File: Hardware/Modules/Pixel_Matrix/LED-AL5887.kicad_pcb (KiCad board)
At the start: 2 copper layers, 35 x 35 mm, 50 parts, among them J1 B4B-EH-A, J2 Conn_01x03_Pin, J3 Conn_01x03_Pin, J4 Conn_01x03_Pin, J5 B6B-EH-A, U1 AL5887JAZW52-13

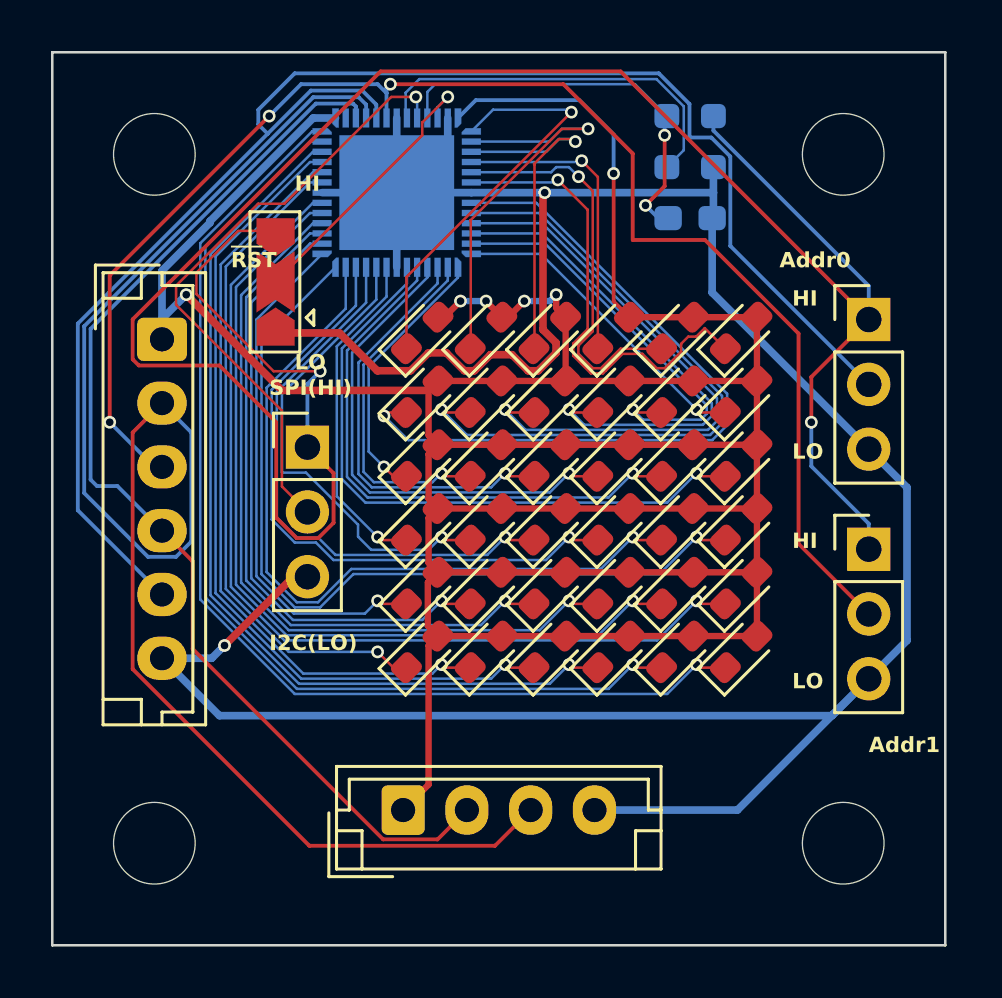
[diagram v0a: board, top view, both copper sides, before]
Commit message: Updated silkscreen
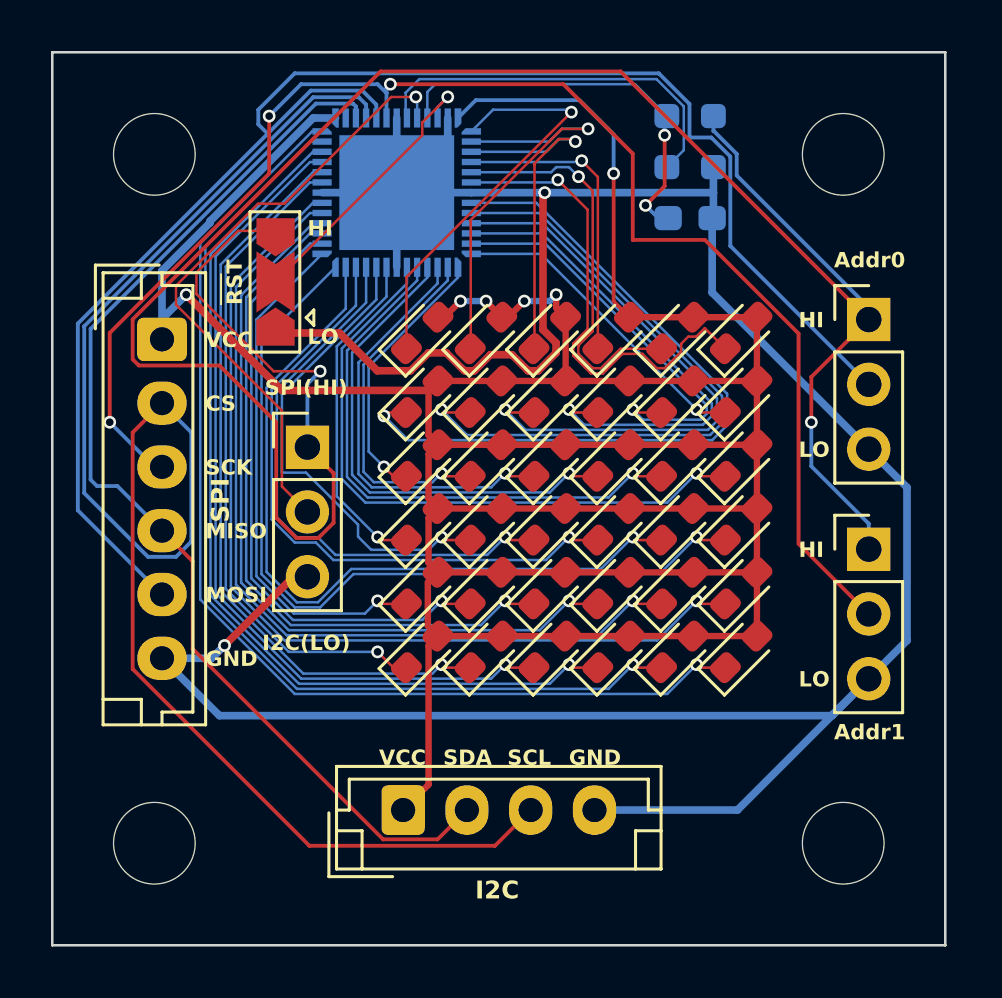
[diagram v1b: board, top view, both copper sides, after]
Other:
- board text added: "C1"
- board text added: "CS"
- board text added: "GND"
- board text added: "I2C"
- board text added: "MISO"
- board text added: "MOSI"
- board text added: "R1"
- board text added: "R2"
- board text added: "SCK"
- board text added: "SCL"
- board text added: "SDA"
- board text added: "SPI"
- board text added: "VCC"

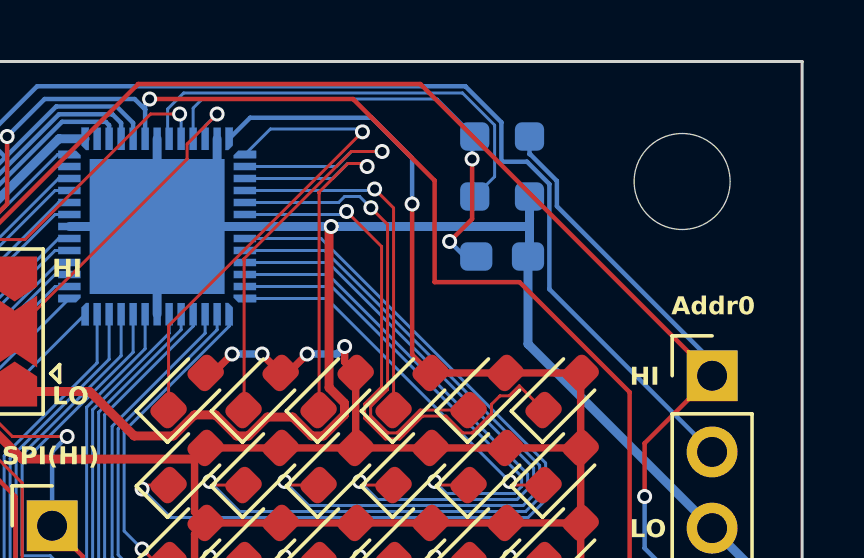
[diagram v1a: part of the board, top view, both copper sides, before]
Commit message: Pin 51 gefixt
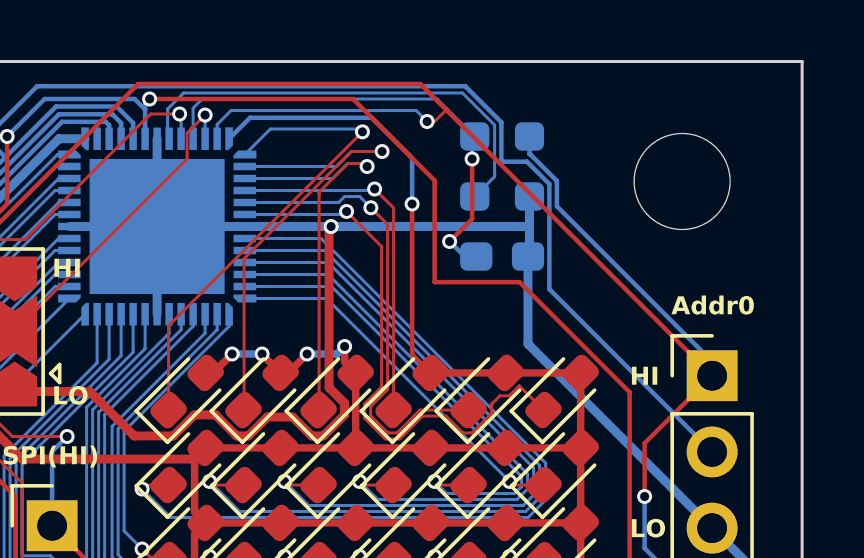
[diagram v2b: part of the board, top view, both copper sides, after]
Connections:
- U1 pad 51: GND -> Net-(J2-Pin_1)
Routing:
- net Net-(J2-Pin_1): track 90.4 -> 99.0 mm, vias 2 -> 3
- net GND: track 117.5 -> 116.5 mm
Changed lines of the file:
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@@
 			(size 0.25 0.75)
 			(layers "B.Cu" "B.Paste")
-			(net 5 "GND")
+			(net 47 "Net-(J2-Pin_1)")
 			(pinfunction "~{EN}")
 			(pintype "input")
@@
 	)
 	(segment
-		(start 74.5 34.075)
-		(end 74.5 35)
-		(width 0.3)
-		(layer "B.Cu")
-		(net 5)
-	)
-	(segment
 		(start 75.425 37)
 		(end 78.3 37)
@@
 	)
 	(segment
+		(start 91 41.975)
+		(end 82.1375 33.1125)
+		(width 0.15)
+		(layer "F.Cu")
+		(net 47)
+	)
+	(segment
 		(start 81.275 32.25)
 		(end 71.867032 32.25)
@@
 	)
 	(segment
-		(start 91 41.975)
-		(end 81.275 32.25)
-		(width 0.15)
+		(start 81.75 33.5)
+		(end 82.1375 33.1125)
+		(width 0.1)
 		(layer "F.Cu")
 		(net 47)
@@
 	)
 	(segment
+		(start 81.5 33.5)
+		(end 81.75 33.5)
+		(width 0.1)
+		(layer "F.Cu")
+		(net 47)
+	)
+	(segment
 		(start 69.424569 50.54)
 		(end 70.025 49.939569)
@@
 	)
 	(segment
+		(start 82.1375 33.1125)
+		(end 81.275 32.25)
+		(width 0.15)
+		(layer "F.Cu")
+		(net 47)
+	)
+	(segment
 		(start 68.575431 50.54)
 		(end 69.424569 50.54)
@@
 	)
 	(via
+		(at 81.5 33.5)
+		(size 0.5)
+		(drill 0.3)
+		(layers "F.Cu" "B.Cu")
+		(net 47)
+	)
+	(via
 		(at 88.75 46)
 		(size 0.5)
@@
 	)
 	(segment
+		(start 74.5 33.6)
+		(end 74.5 34.075)
+		(width 0.1)
+		(layer "B.Cu")
+		(net 47)
+	)
+	(segment
 		(start 84.9125 34)
 		(end 84.9125 34.589944)
@@
 	)
 	(segment
+		(start 74.965012 33.134988)
+		(end 74.5 33.6)
+		(width 0.1)
+		(layer "B.Cu")
+		(net 47)
+	)
+	(segment
 		(start 91 50.975)
 		(end 91 49.975)
@@
 	)
 	(segment
+		(start 81.134988 33.134988)
+		(end 74.965012 33.134988)
+		(width 0.1)
+		(layer "B.Cu")
+		(net 47)
+	)
+	(segment
 		(start 85.825 36.325)
 		(end 91 41.5)
@@
 	)
 	(segment
+		(start 81.5 33.5)
+		(end 81.134988 33.134988)
+		(width 0.1)
+		(layer "B.Cu")
+		(net 47)
+	)
+	(segment
 		(start 84.933442 34.589944)
 		(end 85.825 35.481502)
@@
 	)
 	(segment
-		(start 73.5 34.25)
-		(end 73.5 34.75)
+		(start 73.5 34.75)
+		(end 67.75 40.5)
 		(width 0.1)
 		(layer "F.Cu")
@@
 	)
 	(segment
-		(start 74.5 33.25)
-		(end 73.5 34.25)
+		(start 74.1 33.285356)
+		(end 73.5 33.885356)
 		(width 0.1)
 		(layer "F.Cu")
@@
 	)
 	(segment
-		(start 73.5 34.75)
-		(end 67.75 40.5)
+		(start 73.5 33.885356)
+		(end 73.5 34.75)
 		(width 0.1)
 		(layer "F.Cu")
@@
 	)
 	(via
-		(at 74.5 33.25)
+		(at 74.1 33.285356)
 		(size 0.5)
 		(drill 0.3)
@@
 	)
 	(segment
-		(start 74.1 33.65)
+		(start 74.1 33.285356)
 		(end 74.1 34.075)
 		(width 0.1)
 		(layer "B.Cu")
-		(net 48)
-	)
-	(segment
-		(start 74.5 33.25)
-		(end 74.1 33.65)
-		(width 0.1)
-		(layer "B.Cu")

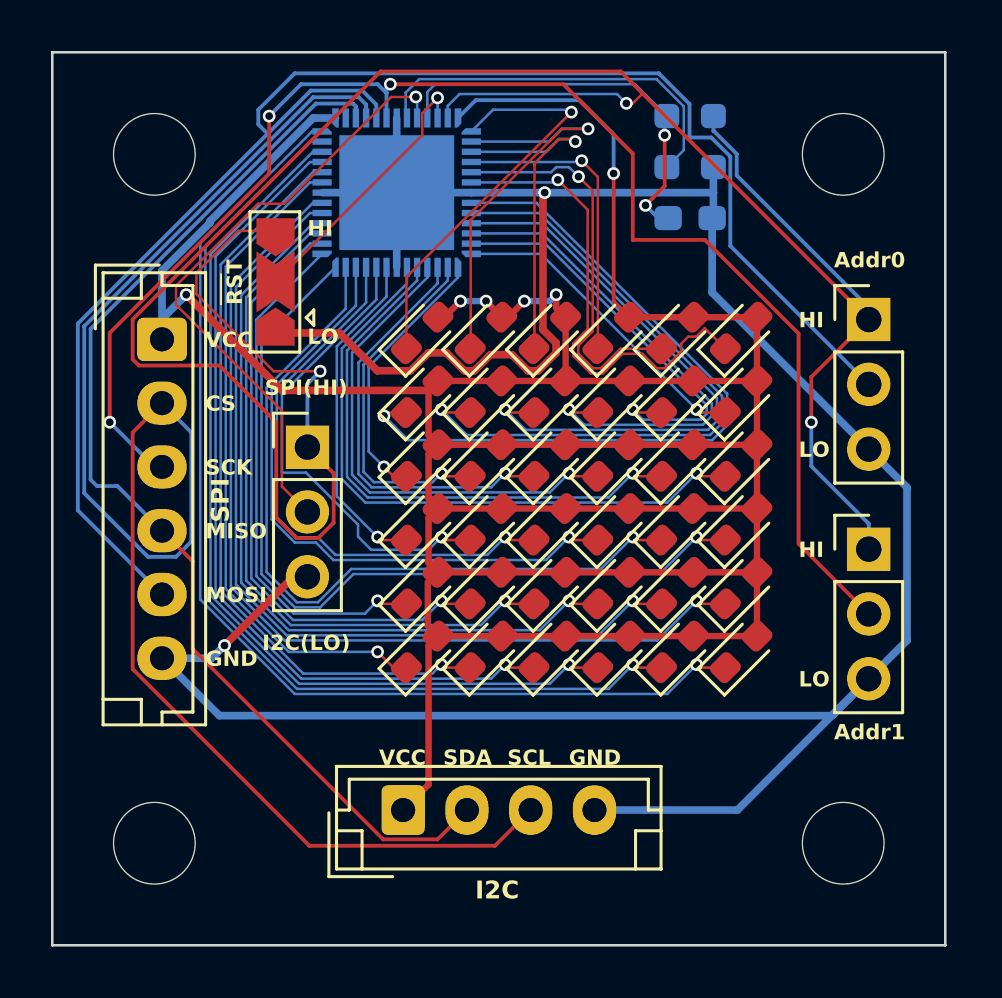
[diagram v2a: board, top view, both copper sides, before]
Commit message: Fixed Pixel matrix
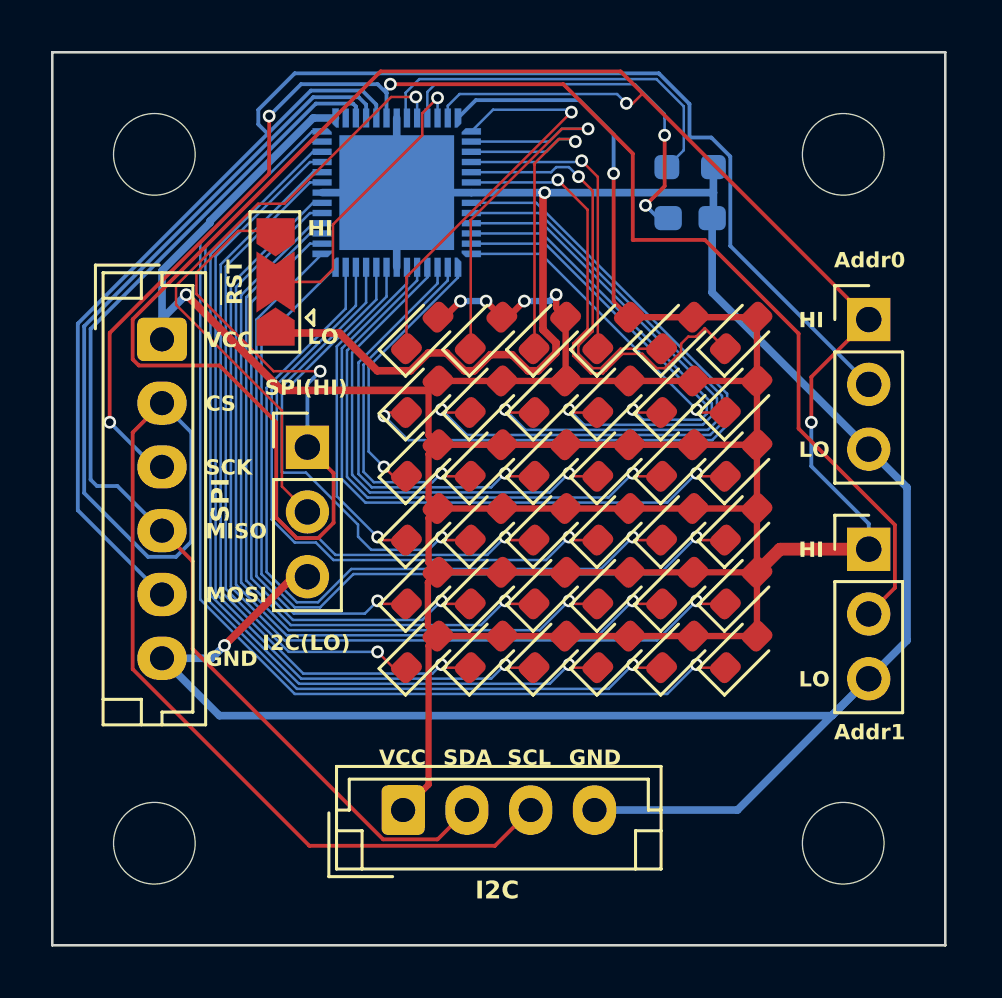
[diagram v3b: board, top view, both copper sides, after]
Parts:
- removed R1: 10k, Resistor_SMD:R_0603_1608Metric_Pad0.98x0.95mm_HandSolder
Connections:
- J2 pad 1: Net-(J2-Pin_1) -> Net-(D1-A)
- J3 pad 1: Net-(J2-Pin_1) -> Net-(D1-A)
- J4 pad 1: Net-(J2-Pin_1) -> Net-(D1-A)
- JP2 pad 3: Net-(J2-Pin_1) -> Net-(D1-A)
- U1 pad 51: Net-(J2-Pin_1) -> Net-(D1-A)
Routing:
- net Net-(J2-Pin_1): track 99.0 -> 0.00 mm, vias 3 -> 0
- net Net-(D1-A): track 147.3 -> 241.0 mm, vias 6 -> 9
- net Net-(JP2-C): track 10.6 -> 11.7 mm
- net Net-(J4-Pin_2): track 58.2 -> 59.0 mm
